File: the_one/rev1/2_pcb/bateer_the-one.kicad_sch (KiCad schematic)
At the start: 0 parts

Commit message: update KiCAD schematcis
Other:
- added sheet e-ink-display (e-ink-display.kicad_sch)
- sheet right-side ports: added E-INK_BUSY, E-INK_CS, E-INK_DC, E-INK_MOSI, E-INK_RST, E-INK_SCK, E-INK_VCC; removed none
- note added: "The left-side's RP2040 board is power supplied by the USB-C cable from the PC."

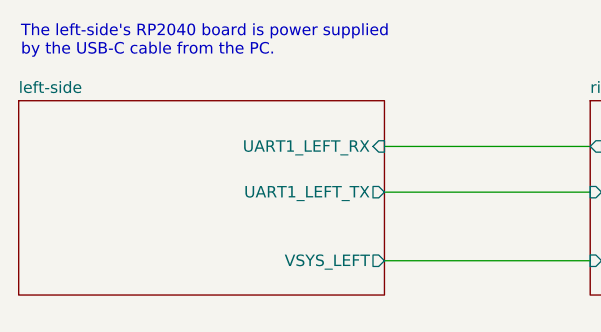
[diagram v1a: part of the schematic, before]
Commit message: add capacitors near e-Ink Vcc pin
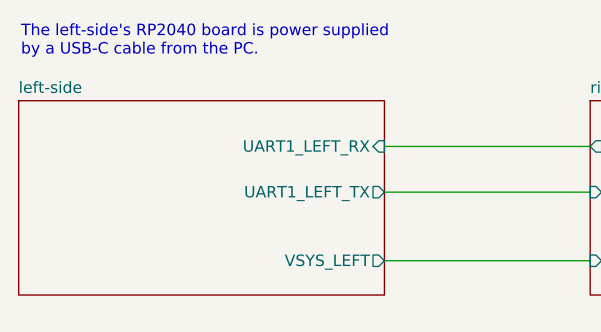
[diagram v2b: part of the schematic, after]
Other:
- note added: "The left-side's RP2040 board is power supplied by a USB-C cable from the PC."
- note removed: "The left-side's RP2040 board is power supplied by the USB-C cable from the PC."
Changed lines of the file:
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@@
 		(company "tuantran39")
 	)
-	(text "The left-side's RP2040 board is power supplied \nby the USB-C cable from the PC."
+	(text "The left-side's RP2040 board is power supplied \nby a USB-C cable from the PC."
 		(exclude_from_sim yes)
 		(at 42.164 25.146 0)

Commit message: update rev1 README
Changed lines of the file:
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@@
+	(wire
+		(pts
+			(xy 82.55 46.99) (xy 105.41 46.99)
+		)
+		(stroke
+			(width 0)
+			(type default)
+		)
+	)
+	(wire
+		(pts
+			(xy 148.59 53.34) (xy 148.59 68.58)
+		)
+		(stroke
+			(width 0)
+			(type default)
+		)
+	)
+	(wire
+		(pts
+			(xy 144.78 53.34) (xy 144.78 68.58)
+		)
+		(stroke
+			(width 0)
+			(type default)
+		)
+	)
+	(wire
+		(pts
+			(xy 82.55 36.83) (xy 105.41 36.83)
+		)
+		(stroke
+			(width 0)
+			(type default)
+		)
+	)
+	(wire
+		(pts
+			(xy 140.97 53.34) (xy 140.97 68.58)
+		)
+		(stroke
+			(width 0)
+			(type default)
+		)
+	)
+	(wire
+		(pts
+			(xy 156.21 53.34) (xy 156.21 68.58)
+		)
+		(stroke
+			(width 0)
+			(type default)
+		)
+	)
+	(wire
+		(pts
+			(xy 137.16 53.34) (xy 137.16 68.58)
+		)
+		(stroke
+			(width 0)
+			(type default)
+		)
+	)
+	(wire
+		(pts
+			(xy 152.4 53.34) (xy 152.4 68.58)
+		)
+		(stroke
+			(width 0)
+			(type default)
+		)
+	)
+	(wire
+		(pts
+			(xy 160.02 53.34) (xy 160.02 68.58)
+		)
+		(stroke
+			(width 0)
+			(type default)
+		)
+	)
 	(wire
 		(pts
 			(xy 82.55 41.91) (xy 105.41 41.91)
-		)
-		(stroke
-			(width 0)
-			(type default)
-		)
-	)
-	(wire
-		(pts
-			(xy 148.59 53.34) (xy 148.59 68.58)
-		)
-		(stroke
-			(width 0)
-			(type default)
-		)
-	)
-	(wire
-		(pts
-			(xy 144.78 53.34) (xy 144.78 68.58)
-		)
-		(stroke
-			(width 0)
-			(type default)
-		)
-	)
-	(wire
-		(pts
-			(xy 82.55 49.53) (xy 105.41 49.53)
-		)
-		(stroke
-			(width 0)
-			(type default)
-		)
-	)
-	(wire
-		(pts
-			(xy 140.97 53.34) (xy 140.97 68.58)
-		)
-		(stroke
-			(width 0)
-			(type default)
-		)
-	)
-	(wire
-		(pts
-			(xy 156.21 53.34) (xy 156.21 68.58)
-		)
-		(stroke
-			(width 0)
-			(type default)
-		)
-	)
-	(wire
-		(pts
-			(xy 137.16 53.34) (xy 137.16 68.58)
-		)
-		(stroke
-			(width 0)
-			(type default)
-		)
-	)
-	(wire
-		(pts
-			(xy 152.4 53.34) (xy 152.4 68.58)
-		)
-		(stroke
-			(width 0)
-			(type default)
-		)
-	)
-	(wire
-		(pts
-			(xy 160.02 53.34) (xy 160.02 68.58)
-		)
-		(stroke
-			(width 0)
-			(type default)
-		)
-	)
-	(wire
-		(pts
-			(xy 82.55 36.83) (xy 105.41 36.83)
 		)
 		(stroke
@@
 		)
 		(pin "UART1_RIGHT_TX" output
+			(at 105.41 41.91 180)
+			(effects
+				(font
+					(size 1.27 1.27)
+				)
+				(justify left)
+			)
+		)
+		(pin "UART1_RIGHT_RX" input
+			(at 105.41 46.99 180)
+			(effects
+				(font
+					(size 1.27 1.27)
+				)
+				(justify left)
+			)
+		)
+		(pin "VSYS_RIGHT" input
 			(at 105.41 36.83 180)
-			(effects
-				(font
-					(size 1.27 1.27)
-				)
-				(justify left)
-			)
-		)
-		(pin "UART1_RIGHT_RX" input
-			(at 105.41 41.91 180)
-			(effects
-				(font
-					(size 1.27 1.27)
-				)
-				(justify left)
-			)
-		)
-		(pin "VSYS_RIGHT" input
-			(at 105.41 49.53 180)
 			(effects
 				(font
@@
 		)
 		(pin "UART1_LEFT_TX" output
+			(at 82.55 46.99 0)
+			(effects
+				(font
+					(size 1.27 1.27)
+				)
+				(justify right)
+			)
+		)
+		(pin "UART1_LEFT_RX" input
 			(at 82.55 41.91 0)
 			(effects
@@
 			)
 		)
-		(pin "UART1_LEFT_RX" input
+		(pin "VSYS_LEFT" output
 			(at 82.55 36.83 0)
 			(effects
 				(font
-					(size 1.27 1.27)
-				)
-				(justify right)
-			)
-		)
-		(pin "VSYS_LEFT" output
-			(at 82.55 49.53 0)
-			(effects
-				(font

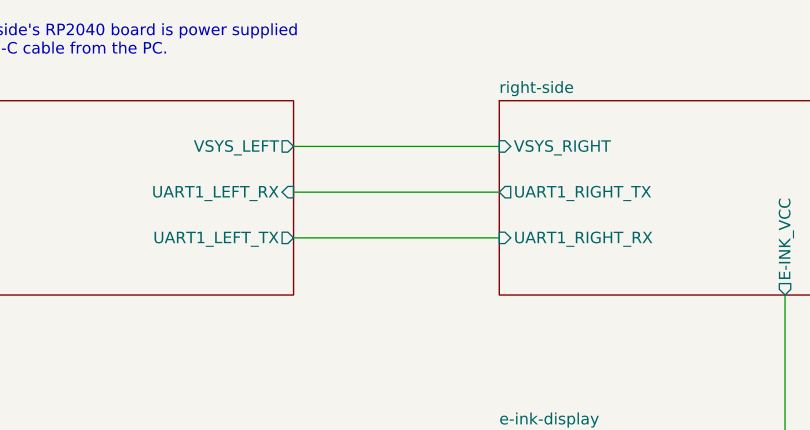
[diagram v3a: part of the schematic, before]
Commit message: change power supply pins of rp2040 from VSYS to VBUS
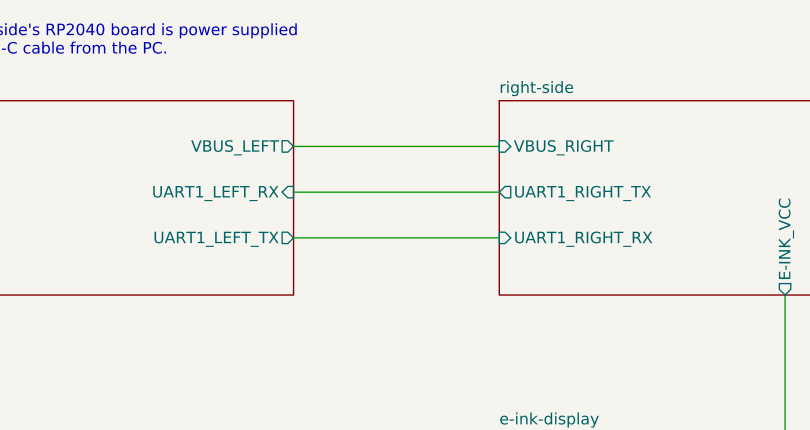
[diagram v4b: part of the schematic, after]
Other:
- sheet left-side ports: added VBUS_LEFT; removed VSYS_LEFT
- sheet right-side ports: added VBUS_RIGHT; removed VSYS_RIGHT
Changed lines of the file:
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@@
 			)
 		)
-		(pin "VSYS_RIGHT" input
+		(pin "VBUS_RIGHT" input
 			(at 105.41 36.83 180)
 			(effects
@@
 			)
 		)
-		(pin "VSYS_LEFT" output
+		(pin "VBUS_LEFT" output
 			(at 82.55 36.83 0)
 			(effects
